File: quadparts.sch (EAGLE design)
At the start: 69 parts, among them J1 AVR_SPI_PRG_6NS, U1 ATMEGA128RFA1, Y1 16MHz

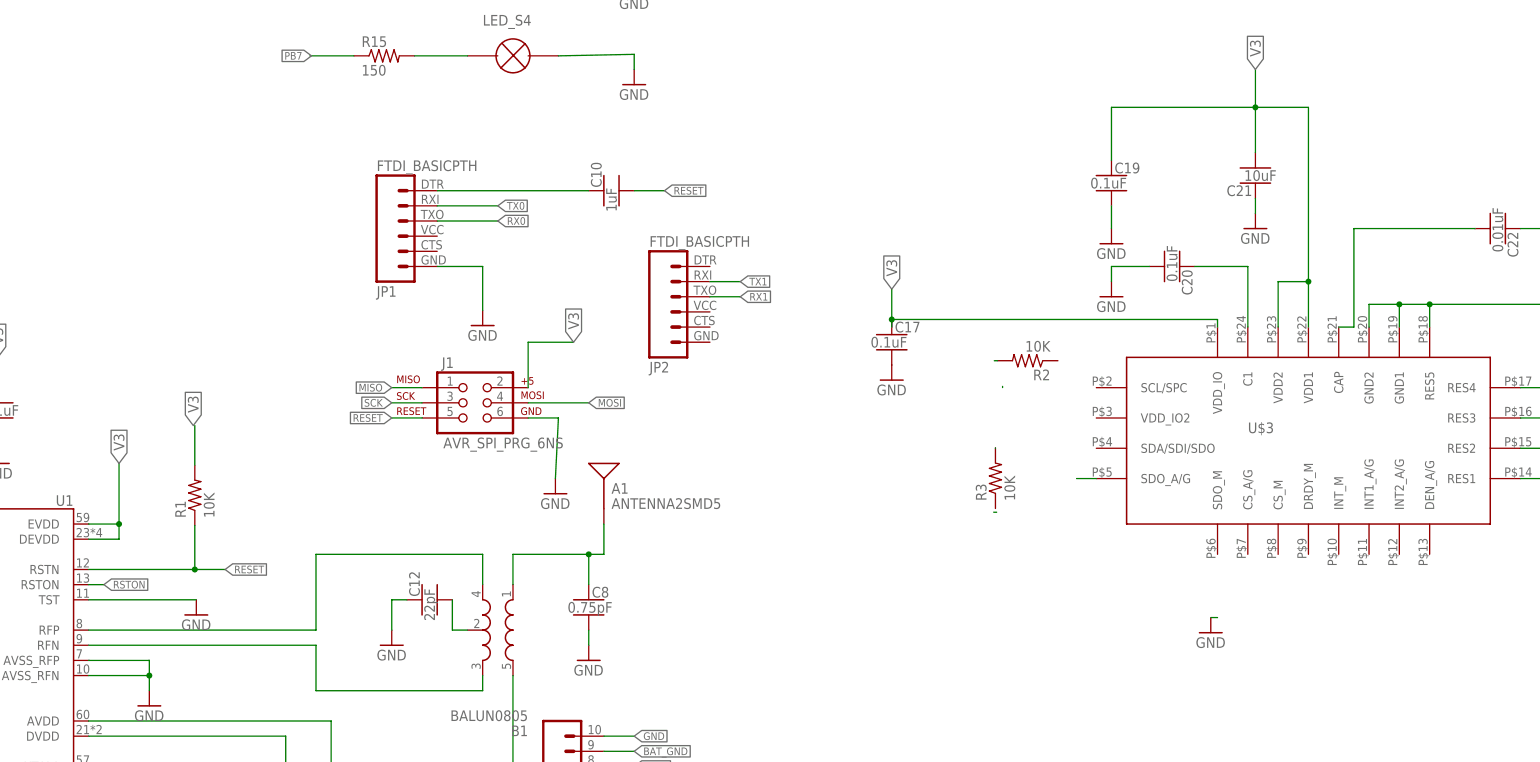
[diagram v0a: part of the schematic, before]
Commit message: Updated IMU
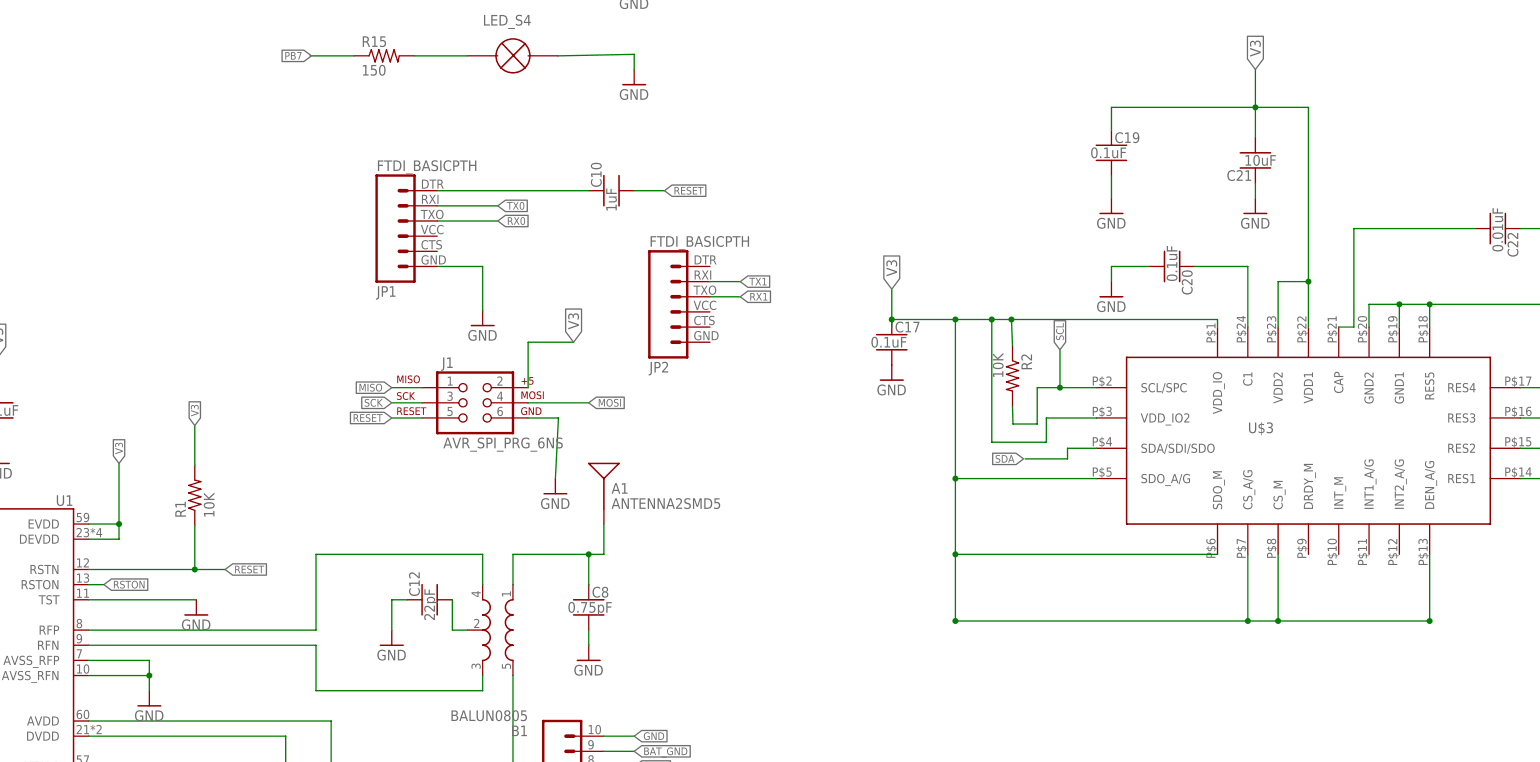
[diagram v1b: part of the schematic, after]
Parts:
- removed R3: 10K, quadparts_prebuilt:RESISTOR_SMD-2012-0805-10K
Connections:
- removed net N$1: R1.2
- removed net N$20: U1.DEVDD, U1.EVDD
- removed net N$30: U$3.SDO_A/G
- removed net N$31: R3.2
- removed net N$34: R2.2
- net SCL: now also R2.2, U$3.SCL/SPC
- net SDA: now also U$3.SDA/SDI/SDO
- net V3: now also R1.2, R2.1, U$3.CS_A/G, U$3.CS_M, U$3.DEN_A/G, U$3.SDO_A/G, U$3.SDO_M, U$3.VDD_IO2, U1.DEVDD, U1.EVDD
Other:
- moved on the sheet: C19, C21, R2

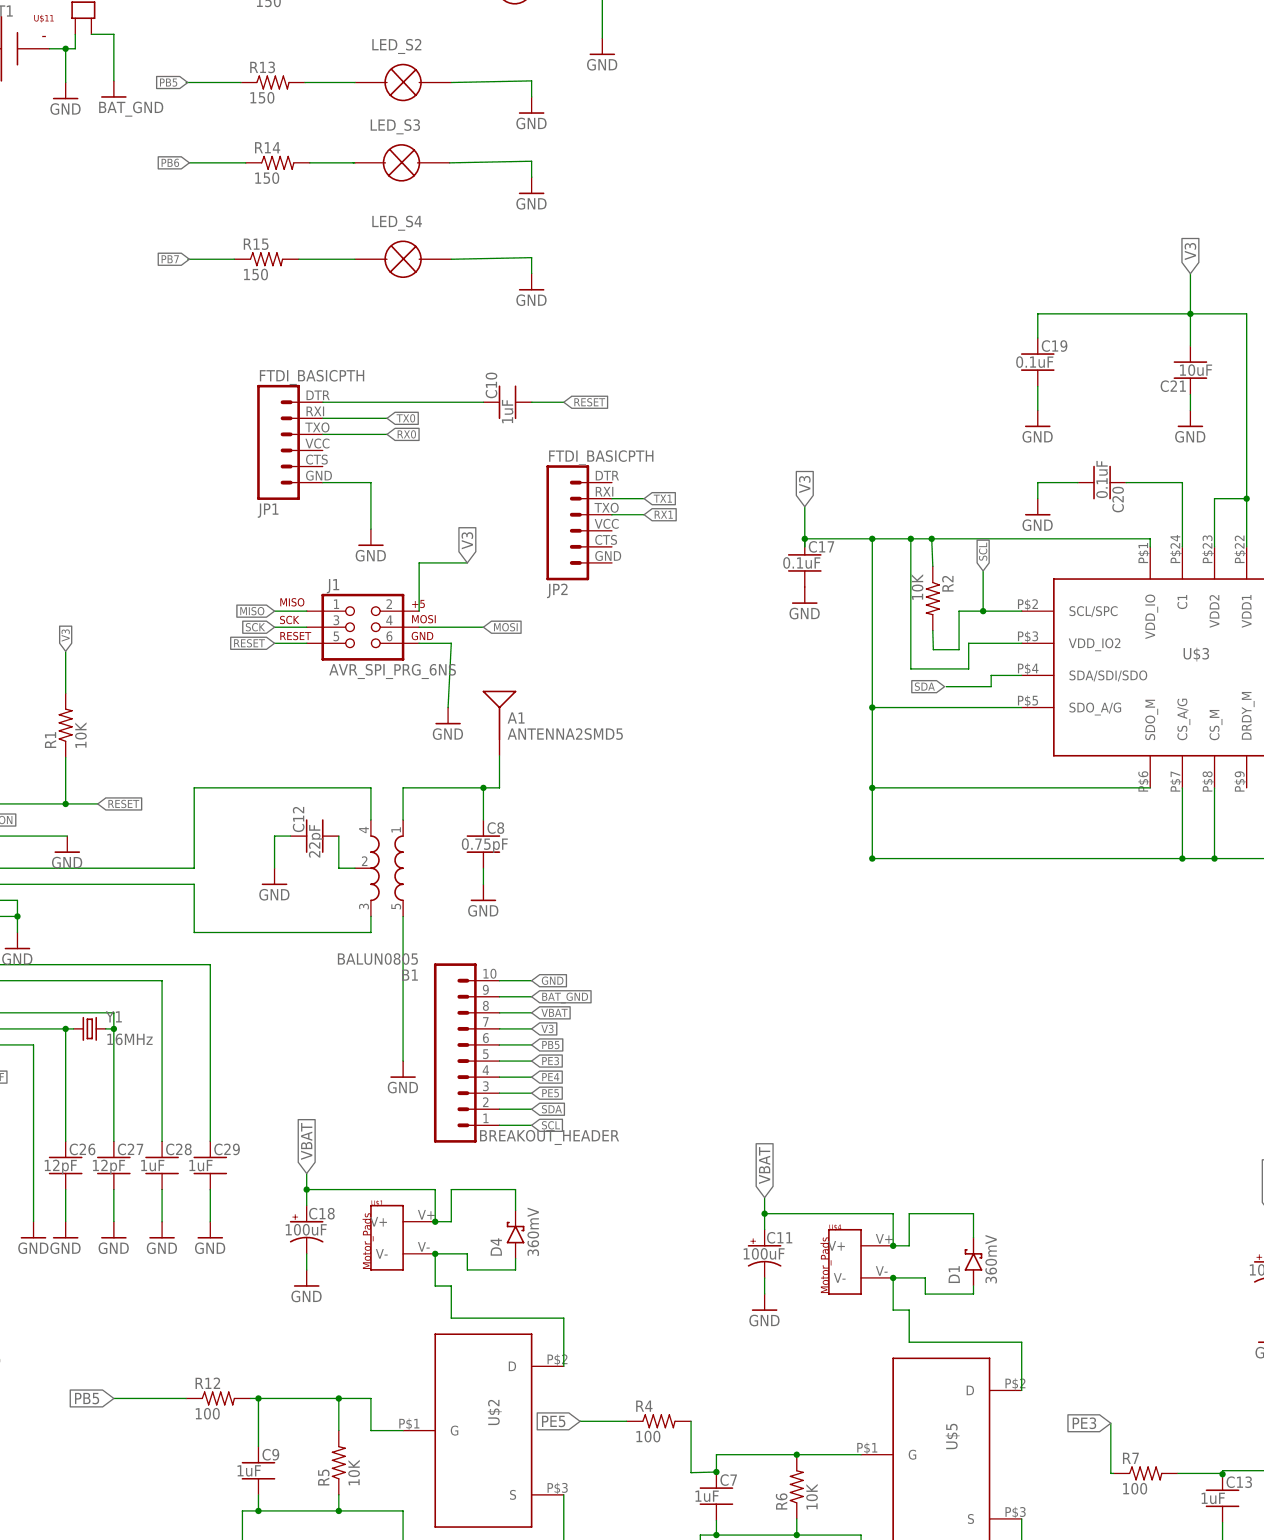
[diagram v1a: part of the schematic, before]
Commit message: Fixed junctions and pull up resistor
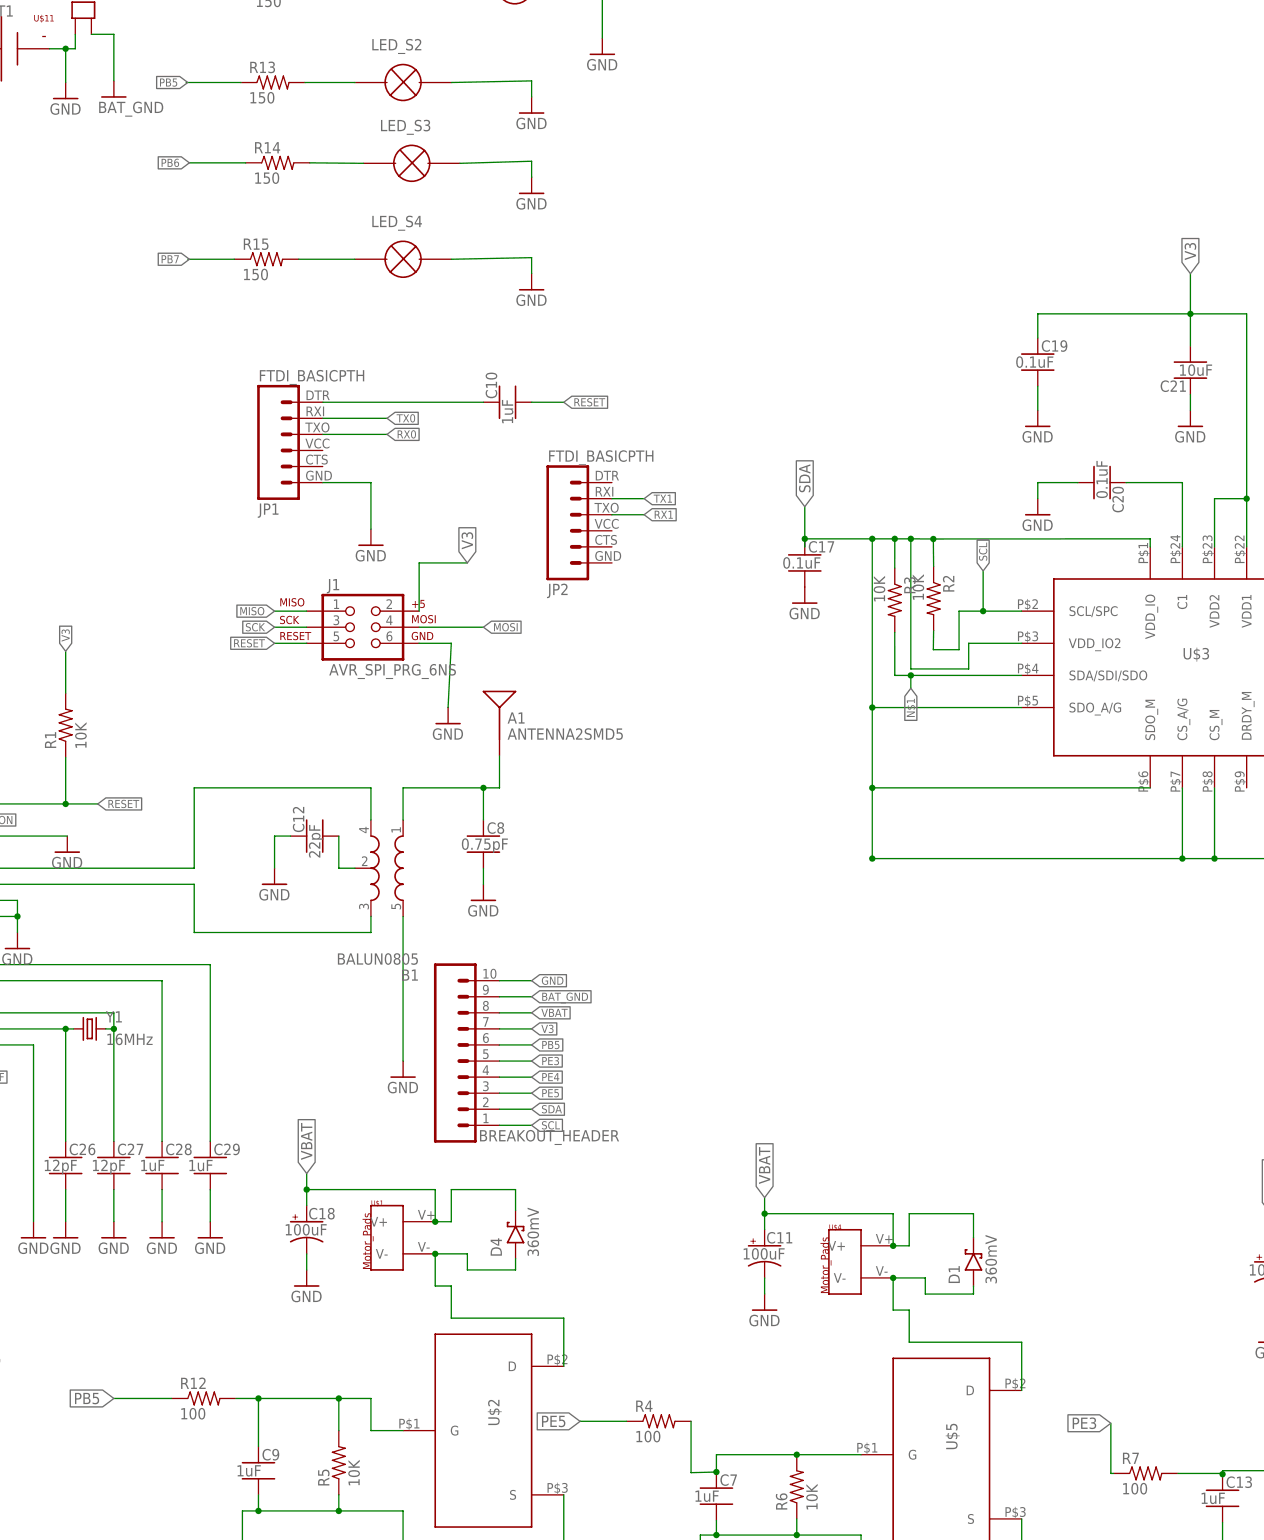
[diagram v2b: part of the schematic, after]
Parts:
- added R3: 10K, quadparts_prebuilt:RESISTOR_SMD-2012-0805-10K
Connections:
- new net N$1: R3.2, U$3.SDA/SDI/SDO
- net SDA: now also C17.1, R2.1, R3.1, U$3.CS_A/G, U$3.CS_M, U$3.DEN_A/G, U$3.SDO_A/G, U$3.SDO_M, U$3.VDD_IO, U$3.VDD_IO2; no longer U$3.SDA/SDI/SDO
- net V3: no longer C17.1, R2.1, U$3.CS_A/G, U$3.CS_M, U$3.DEN_A/G, U$3.SDO_A/G, U$3.SDO_M, U$3.VDD_IO, U$3.VDD_IO2
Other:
- moved on the sheet: LED_S3, R12
